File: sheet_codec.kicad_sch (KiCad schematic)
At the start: 21 parts, among them J3 Carrier LEFT 1-7, J4 Carrier RIGHT 1-7, J6 I2C 3V3/AGND/SDA/SCL, U1 ES8389, U2 TPS7A2033

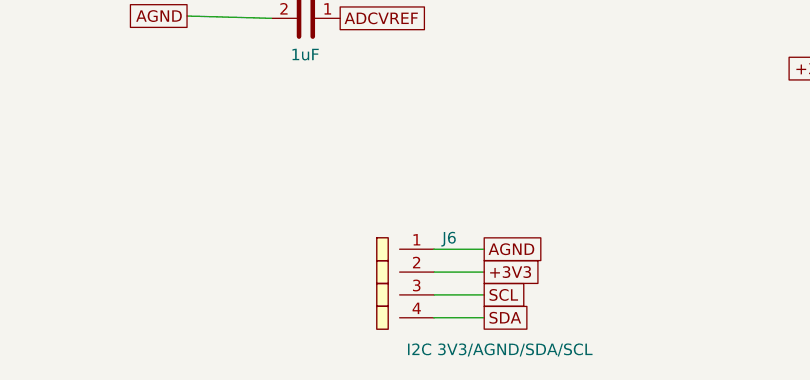
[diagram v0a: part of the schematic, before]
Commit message: pcb: input-corridor tweaks; J6 display header now DNP; regen fab + docs
- J6 hand-fit per build; eurorack builds don't need it at all (the
  Synthia interposer drives the display directly from its own socket)
- BOM: J6 marked DNP; fab assembly split updated (JLC THT = J3/J4 only;
  CPL 69 placed, 9 exclusions: C19 J1 J2 J5 J6 J7 R14 R27 SW1)
- restore exclude_from_pos flags wiped by layout sessions
- README: power/host notes (USB-C + PoE concurrency, hot-plug pop,
  USB-only bench), brackets/ and docs/ in repo layout
- regen gerbers/BOM/CPL, doc PDFs, board STEP
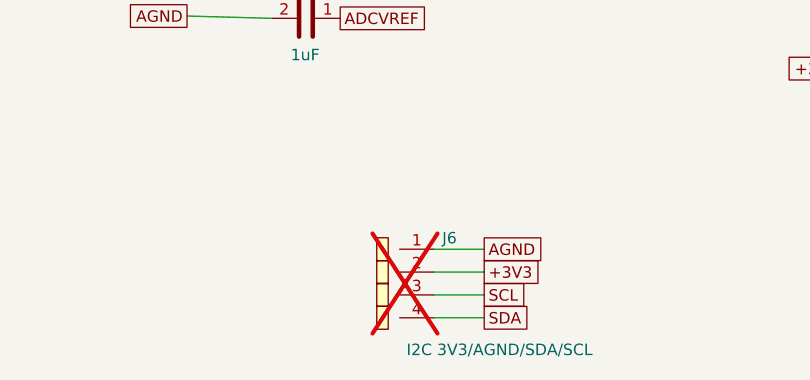
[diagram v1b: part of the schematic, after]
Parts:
- J6: now not fitted
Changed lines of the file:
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@@
 		(on_board yes)
 		(in_pos_files yes)
-		(dnp no)
+		(dnp yes)
 		(property "Reference" "J6"
 			(at 250.602 188 0)

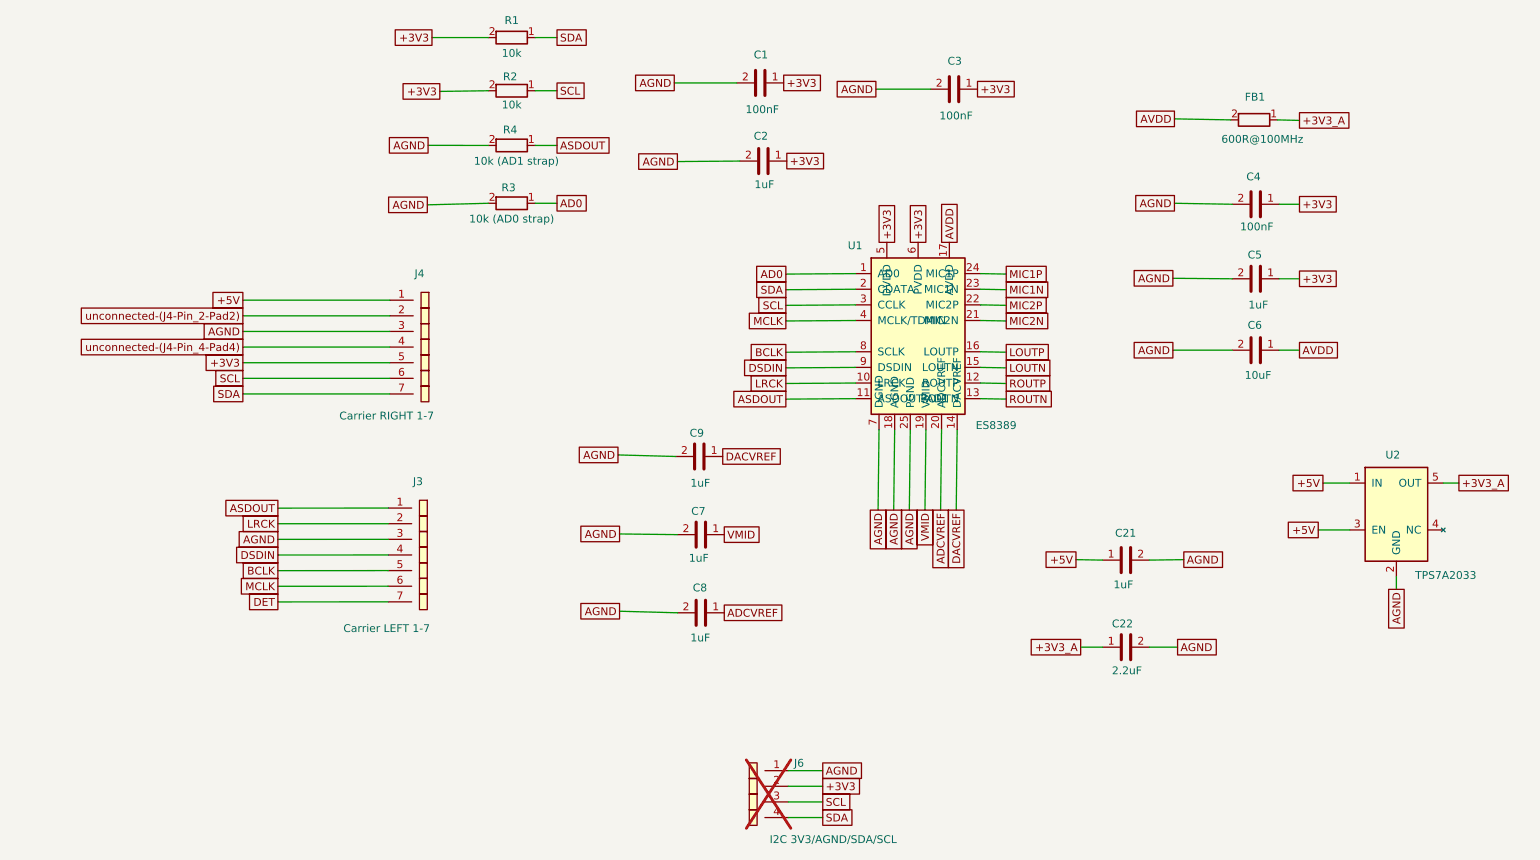
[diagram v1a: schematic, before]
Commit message: sch+pcb: dual-host mezzanine pinout (ESP32-P4 + Pico) — I2C to J3.1/2, BCLK/LRCK adjacent, MCLK/DET on J4.6/7, new R28 MCLK series link; regen fab + docs; add pinout graphic
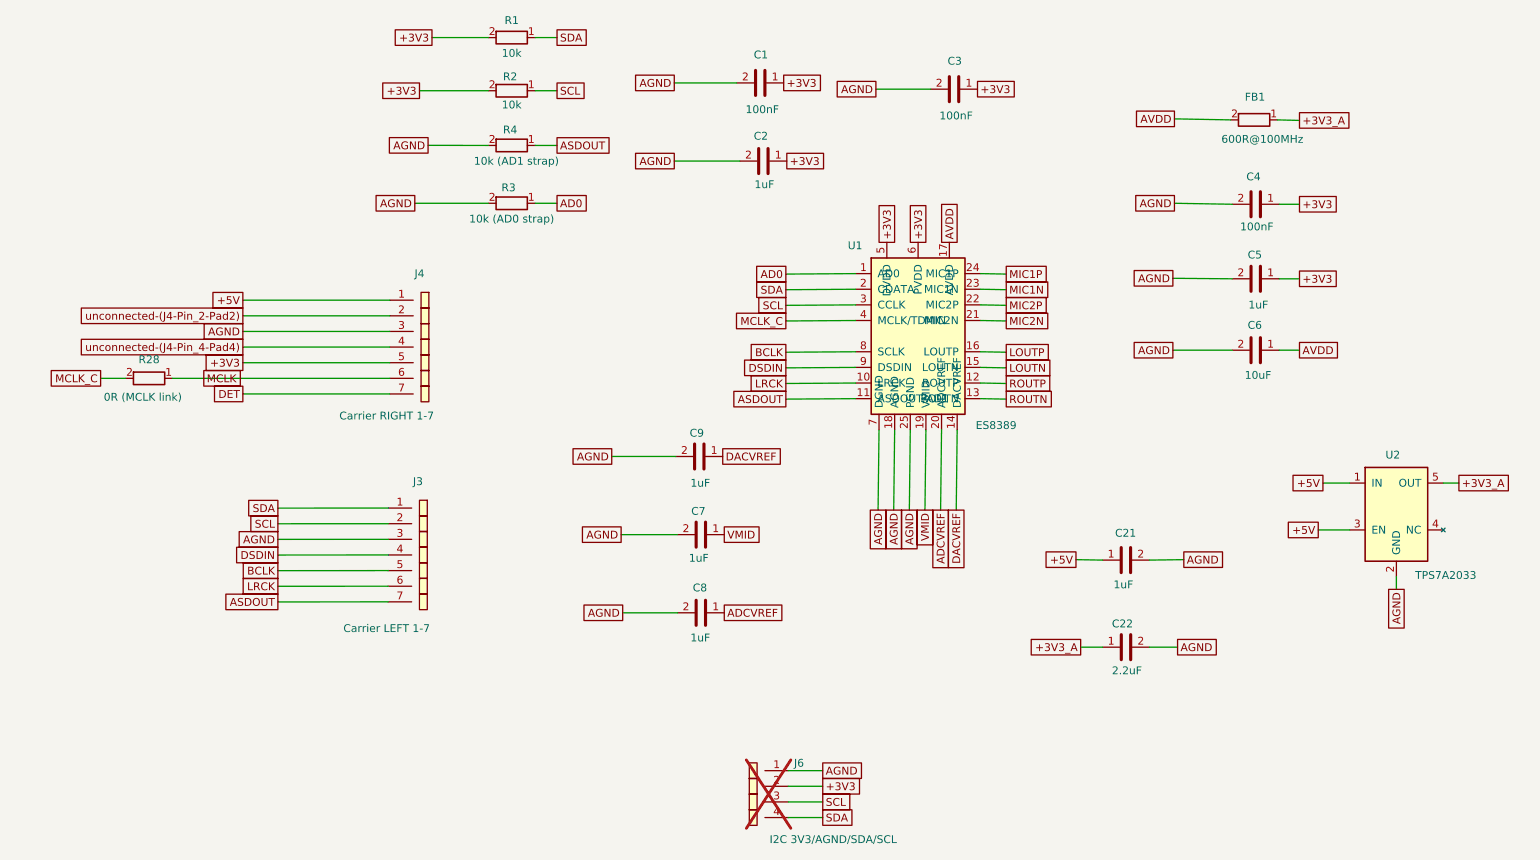
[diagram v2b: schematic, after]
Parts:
- added R28: 0R (MCLK link), Resistor_SMD:R_0805_2012Metric, symbol scramble_hat:R
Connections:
- net ASDOUT: now also J3.7 (Pin_7); no longer J3.1 (Pin_1)
- net DET: now also J4.7 (Pin_7); no longer J3.7 (Pin_7)
- net LRCK: now also J3.6 (Pin_6); no longer J3.2 (Pin_2)
- net MCLK: now also J4.6 (Pin_6), R28.1; no longer J3.6 (Pin_6), U1.4 (MCLK/TDMIN)
- net SCL: now also J3.2 (Pin_2); no longer J4.6 (Pin_6)
- net SDA: now also J3.1 (Pin_1); no longer J4.7 (Pin_7)
- new net MCLK_C: R28.2, U1.4 (MCLK/TDMIN)
